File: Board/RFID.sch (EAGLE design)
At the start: 24 parts, among them IC1 B82450A1084C000, Q8 125kHz, U1 HTRC11001T/02EE,11

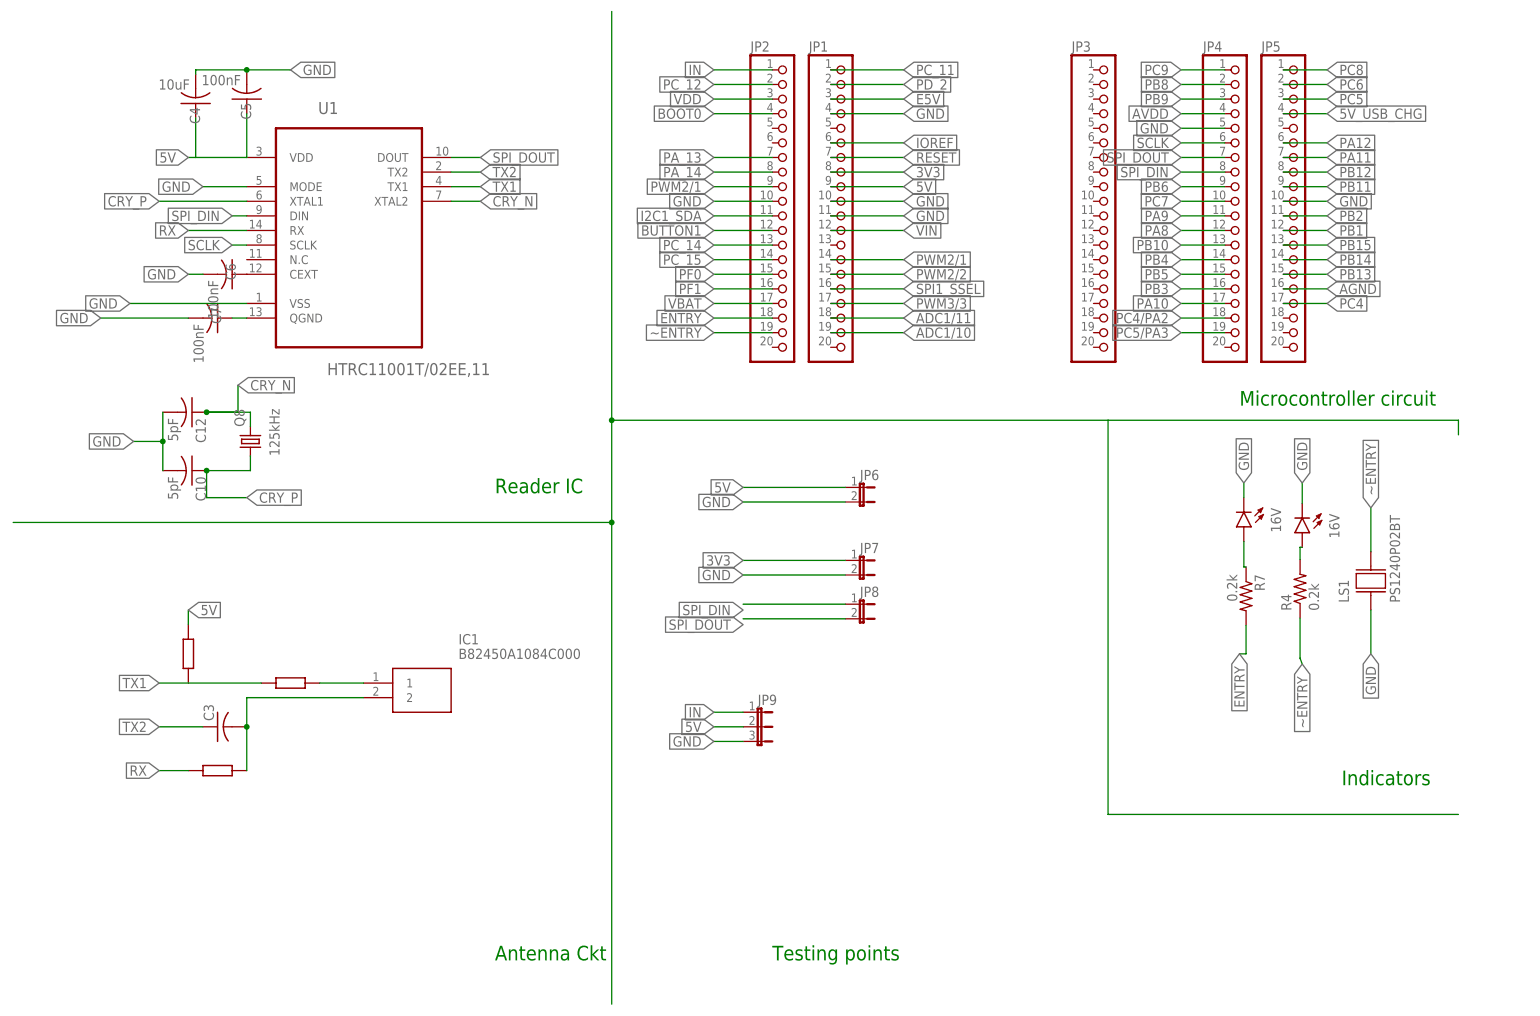
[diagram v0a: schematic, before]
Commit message: Placed board iter1
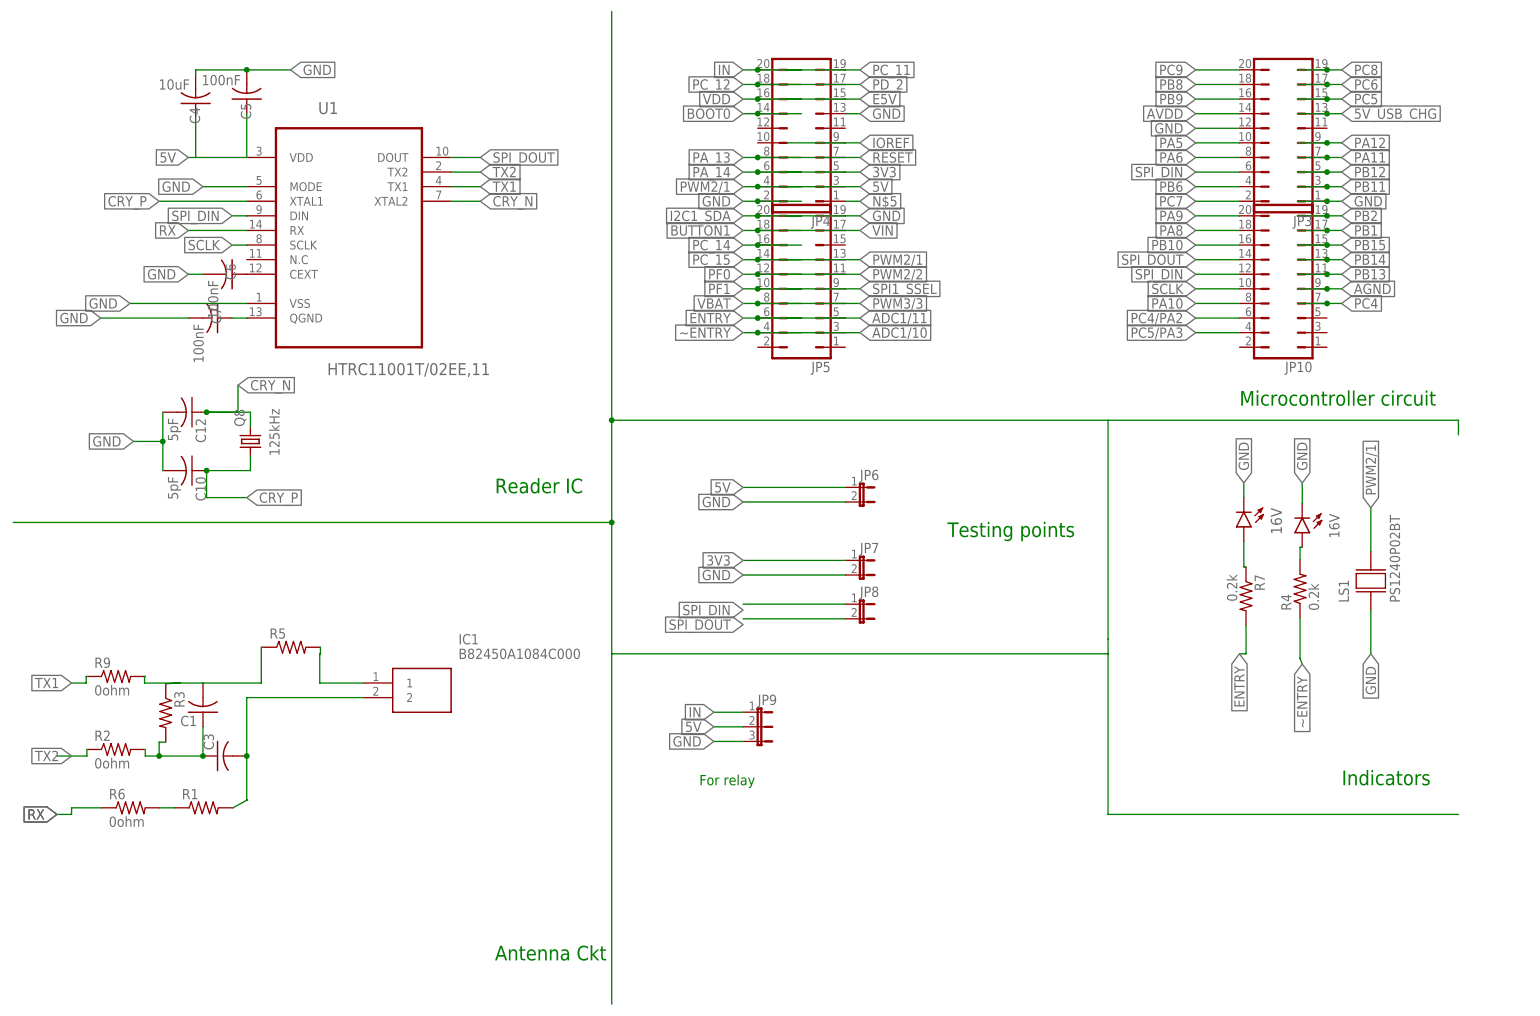
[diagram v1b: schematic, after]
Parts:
- removed JP1, JP2: (no value), adafruit:PINHD-1X20
- added C1: (no value), rcl:C-USC0805
- added JP10: (no value), jumper:JP10Q
- added R1, R3, R5: (no value), adafruit:R-US_R0603
- added R2, R6, R9: 0ohm, adafruit:R-US_R0603
- JP3, JP4, JP5: device adafruit:PINHD-1X20 -> jumper:JP10Q
- renumbered GPIO_5V to RLED, GPIO_POWER to GLED
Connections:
- removed net PB3: JP4.16
- removed net PB4: JP4.14
- removed net PB5: JP4.15
- new net ANT3: C1.1, C3.1, R2.2, R3.2
- new net N$4: R1.1, R6.2
- new net N$5: JP4.1
- new net PA5: JP3.10
- new net PA6: JP3.8
- net 3V3: now also JP4.5; no longer JP1.8
- net 5V: now also JP4.3; no longer JP1.9
- net 5V_USB_CHG: now also JP3.13; no longer JP5.4
- net ADC1/10: now also JP5.3; no longer JP1.19
- net ADC1/11: now also JP5.5; no longer JP1.18
- net AGND: now also JP10.9; no longer JP5.16
- net ANT1: now also R5.2
- net ANT2: now also R1.2
- net AVDD: now also JP3.14; no longer JP4.4
- net BOOT0: now also JP4.14; no longer JP2.4
- net BUTTON1: now also JP5.18; no longer JP2.12
- net E5V: now also JP4.15; no longer JP1.3
- net ENTRY: now also JP5.6; no longer JP2.18
- net GND: now also JP3.1, JP3.12, JP4.13, JP4.2, JP5.19; no longer JP1.10, JP1.11, JP1.4, JP2.10, JP4.5, JP5.10
- net I2C1_SDA: now also JP5.20; no longer JP2.11
- net IN: now also JP4.20; no longer JP2.1
- net IOREF: now also JP4.9; no longer JP1.6
- net PA10: now also JP10.8; no longer JP4.17
- net PA11: now also JP3.7; no longer JP5.7
- net PA12: now also JP3.9; no longer JP5.6
- net PA8: now also JP10.18; no longer JP4.12
- net PA9: now also JP10.20; no longer JP4.11
- net PA_13: now also JP4.8; no longer JP2.7
- net PA_14: now also JP4.6; no longer JP2.8
- net PB1: now also JP10.17; no longer JP5.12
- net PB10: now also JP10.16; no longer JP4.13
- net PB11: now also JP3.3; no longer JP5.9
- net PB12: now also JP3.5; no longer JP5.8
- net PB13: now also JP10.11; no longer JP5.15
- net PB14: now also JP10.13; no longer JP5.14
- net PB15: now also JP10.15; no longer JP5.13
- net PB2: now also JP10.19; no longer JP5.11
- net PB6: now also JP3.4; no longer JP4.9
- net PB8: now also JP3.18; no longer JP4.2
- net PB9: now also JP3.16; no longer JP4.3
- net PC4: now also JP10.7; no longer JP5.17
- net PC4/PA2: now also JP10.6; no longer JP4.18
- net PC5: now also JP3.15; no longer JP5.3
- net PC5/PA3: now also JP10.4; no longer JP4.19
- net PC6: now also JP3.17; no longer JP5.2
- net PC7: now also JP3.2; no longer JP4.10
- net PC8: now also JP3.19; no longer JP5.1
- net PC9: now also JP3.20; no longer JP4.1
- net PC_11: now also JP4.19; no longer JP1.1
- net PC_12: now also JP4.18; no longer JP2.2
- net PC_14: now also JP5.16; no longer JP2.13
- net PC_15: now also JP5.14; no longer JP2.14
- net PD_2: now also JP4.17; no longer JP1.2
- net PF0: now also JP5.12; no longer JP2.15
- net PF1: now also JP5.10; no longer JP2.16
- net PWM2/1: now also JP4.4, JP5.13, LS1.2; no longer JP1.14, JP2.9
- net PWM2/2: now also JP5.11; no longer JP1.15
- net PWM3/3: now also JP5.7; no longer JP1.17
- net RESET: now also JP4.7; no longer JP1.7
- net RX: now also R6.1
- net SCLK: now also JP10.10; no longer JP4.6
- net SPI1_SSEL: now also JP5.9; no longer JP1.16
- net SPI_DIN: now also JP10.12, JP3.6; no longer JP4.8
- net SPI_DOUT: now also JP10.14; no longer JP4.7
- net TX1: now also C1.2, R3.1, R5.1, R9.1, R9.2
- net TX2: now also R2.1; no longer C3.1
- net VBAT: now also JP5.8; no longer JP2.17
- net VDD: now also JP4.16; no longer JP2.3
- net VIN: now also JP5.17; no longer JP1.12
- net ~ENTRY: now also JP5.4; no longer JP2.19, LS1.2
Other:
- note added: "For relay"
- moved on the sheet: C3
